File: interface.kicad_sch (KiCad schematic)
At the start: 4 parts

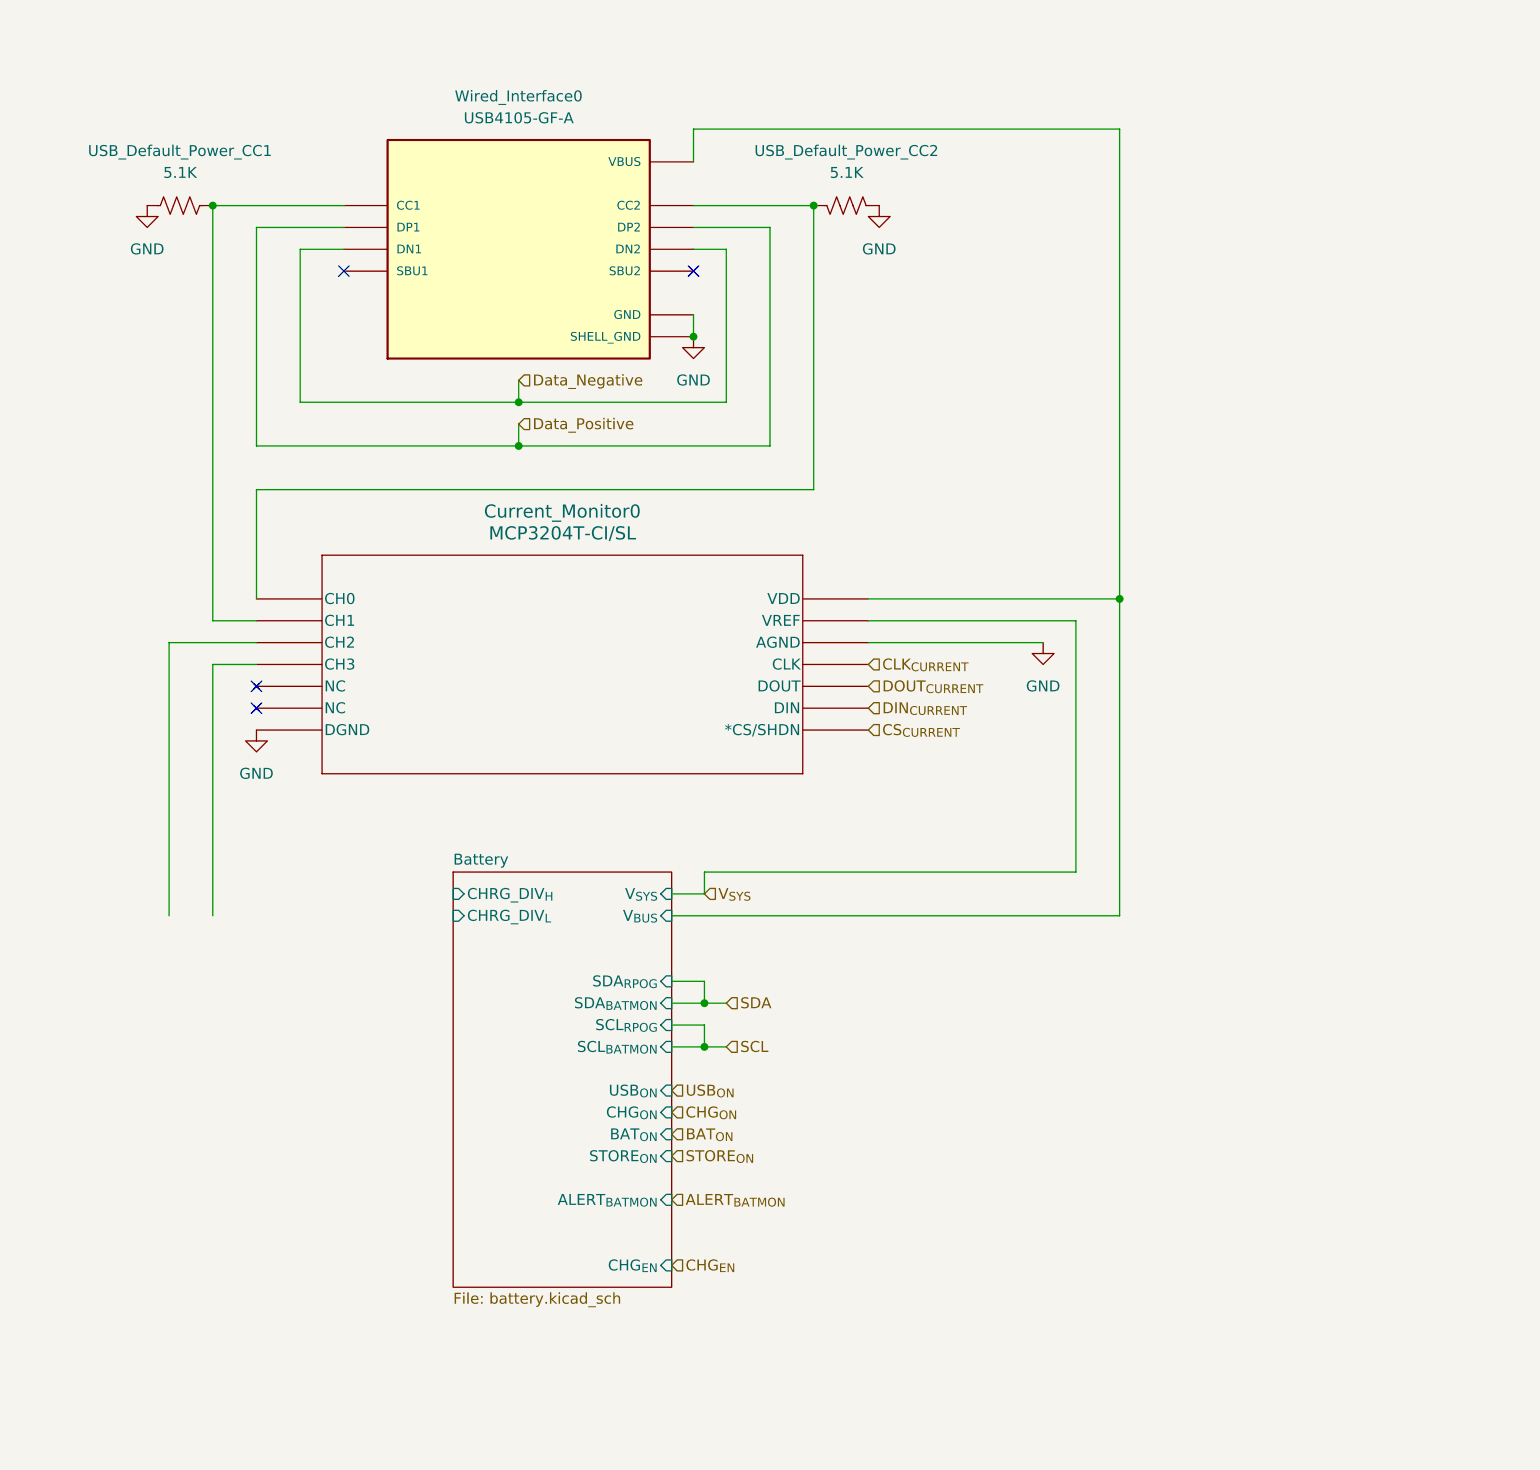
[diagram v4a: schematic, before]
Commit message: Complete most of RHS layout
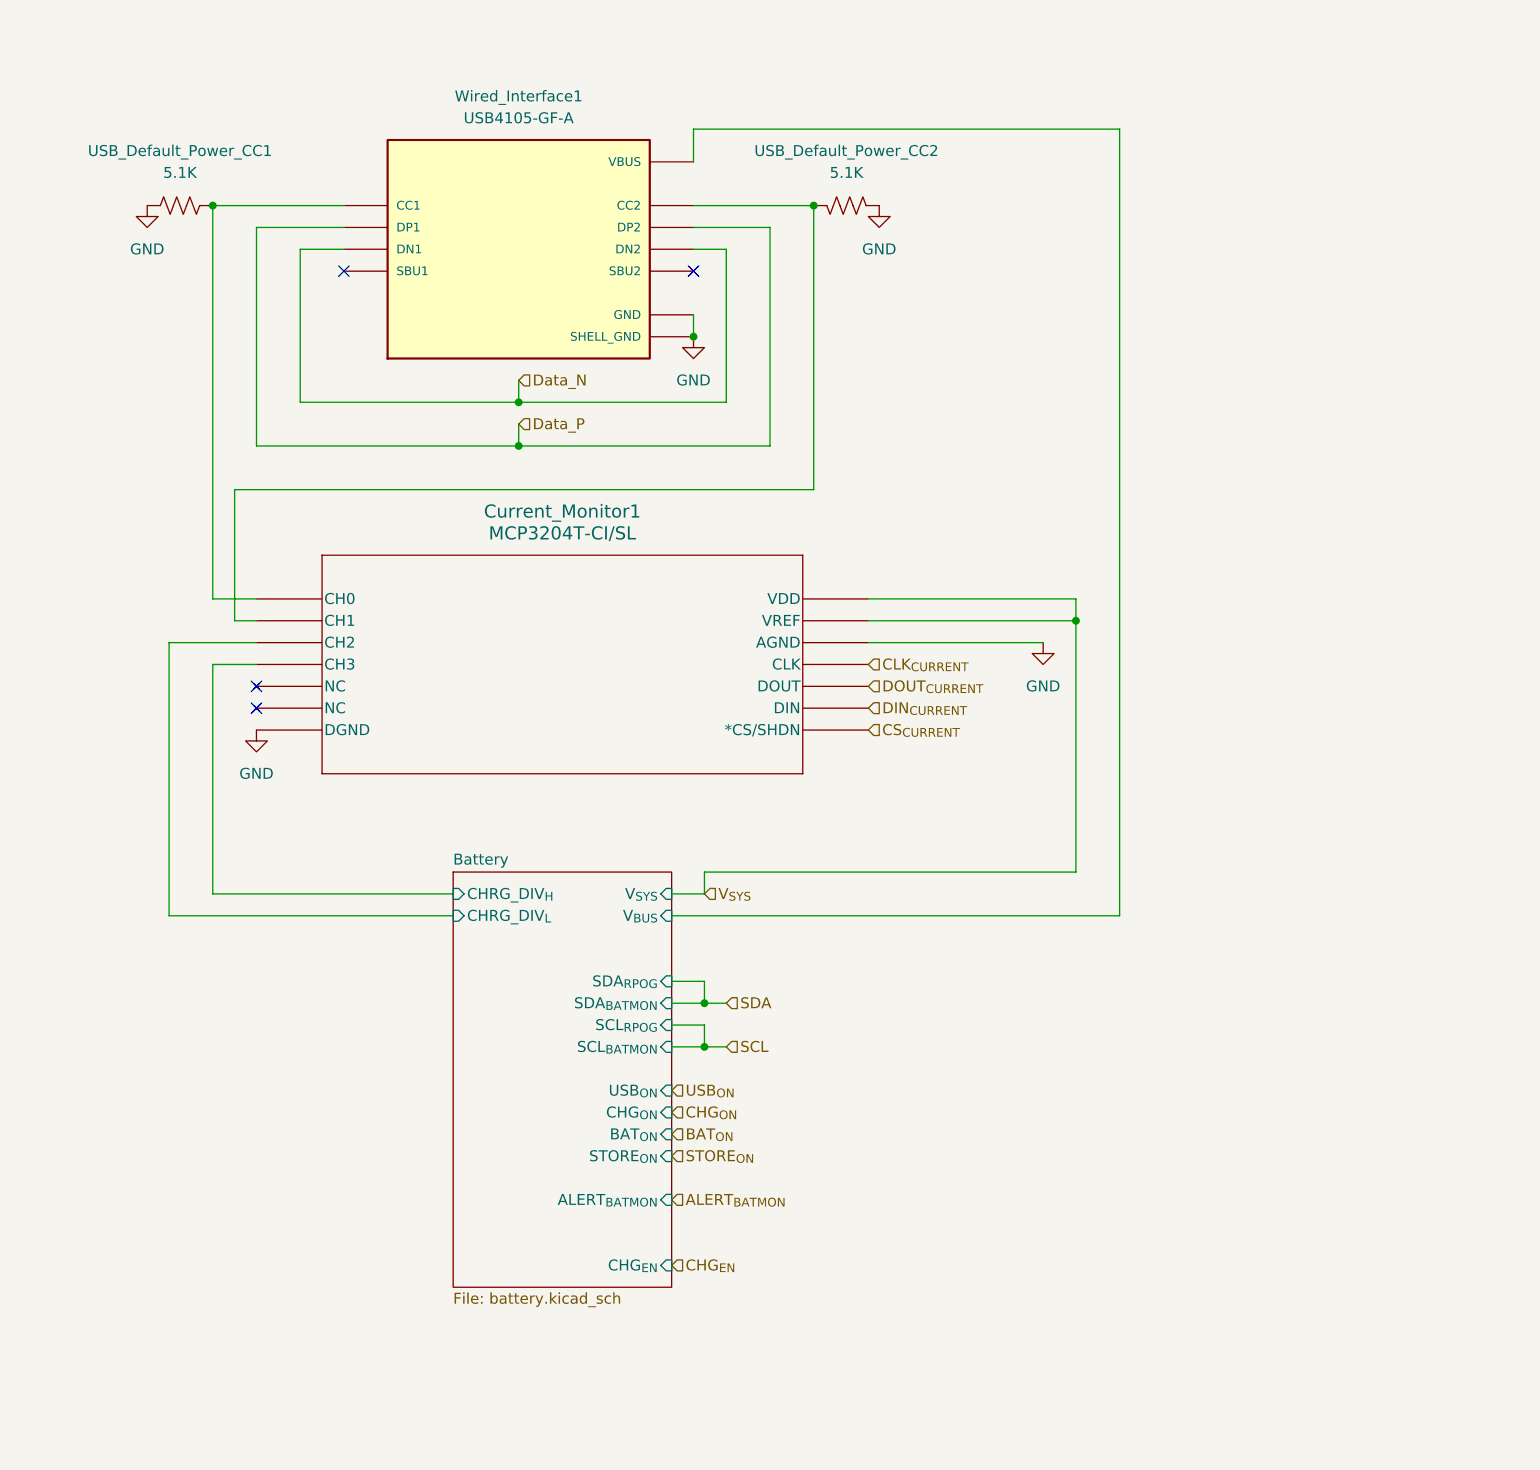
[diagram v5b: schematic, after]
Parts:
- renumbered Current_Monitor0 to Current_Monitor1, Wired_Interface0 to Wired_Interface1
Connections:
- net Battery/CHRG_DIV_{H}: now also Current_Monitor1.4 (CH3)
- net Battery/CHRG_DIV_{L}: now also Current_Monitor1.3 (CH2)
- net Battery/V_{BUS}: no longer Current_Monitor1.14 (VDD)
- net V_{SYS}: now also Current_Monitor1.14 (VDD)
- net at USB_Default_Power_CC1.1, Wired_Interface1.A5 (CC1): now also Current_Monitor1.1 (CH0); no longer Current_Monitor1.2 (CH1)
- net at USB_Default_Power_CC2.1, Wired_Interface1.B5 (CC2): now also Current_Monitor1.2 (CH1); no longer Current_Monitor1.1 (CH0)
- net Data_Negative renamed Data_N
- net Data_Positive renamed Data_P
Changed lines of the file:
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@@
-	)
-	(junction
-		(at 214.63 87.63)
-		(diameter 0)
-		(color 0 0 0 0)
 	)
 	(junction
@@
 	)
 	(junction
+		(at 209.55 90.17)
+		(diameter 0)
+		(color 0 0 0 0)
+	)
+	(junction
 		(at 144.78 64.77)
 		(diameter 0)
@@
 	(wire
 		(pts
-			(xy 114.3 87.63) (xy 114.3 74.93)
-		)
-		(stroke
-			(width 0)
-			(type default)
-		)
-	)
-	(wire
-		(pts
 			(xy 104.14 92.71) (xy 104.14 124.46)
 		)
@@
 	(wire
 		(pts
+			(xy 114.3 90.17) (xy 111.76 90.17)
+		)
+		(stroke
+			(width 0)
+			(type default)
+		)
+	)
+	(wire
+		(pts
+			(xy 109.22 87.63) (xy 114.3 87.63)
+		)
+		(stroke
+			(width 0)
+			(type default)
+		)
+	)
+	(wire
+		(pts
 			(xy 165.1 41.91) (xy 179.07 41.91)
 		)
@@
 	(wire
 		(pts
+			(xy 104.14 124.46) (xy 137.16 124.46)
+		)
+		(stroke
+			(width 0)
+			(type default)
+		)
+	)
+	(wire
+		(pts
+			(xy 111.76 74.93) (xy 179.07 74.93)
+		)
+		(stroke
+			(width 0)
+			(type default)
+		)
+	)
+	(wire
+		(pts
 			(xy 124.46 46.99) (xy 119.38 46.99)
 		)
@@
 	(wire
 		(pts
-			(xy 109.22 95.25) (xy 109.22 124.46)
+			(xy 109.22 95.25) (xy 109.22 121.92)
 		)
 		(stroke
@@
 	(wire
 		(pts
-			(xy 114.3 74.93) (xy 179.07 74.93)
-		)
-		(stroke
-			(width 0)
-			(type default)
-		)
-	)
-	(wire
-		(pts
 			(xy 209.55 119.38) (xy 209.55 90.17)
 		)
@@
 	(wire
 		(pts
+			(xy 109.22 87.63) (xy 109.22 41.91)
+		)
+		(stroke
+			(width 0)
+			(type default)
+		)
+	)
+	(wire
+		(pts
 			(xy 162.56 134.62) (xy 166.37 134.62)
 		)
@@
 	(wire
 		(pts
-			(xy 214.63 87.63) (xy 214.63 124.46)
-		)
-		(stroke
-			(width 0)
-			(type default)
-		)
-	)
-	(wire
-		(pts
 			(xy 166.37 134.62) (xy 168.91 134.62)
 		)
@@
 	(wire
 		(pts
-			(xy 185.42 87.63) (xy 214.63 87.63)
-		)
-		(stroke
-			(width 0)
-			(type default)
-		)
-	)
-	(wire
-		(pts
 			(xy 165.1 33.02) (xy 165.1 36.83)
 		)
@@
 	(wire
 		(pts
+			(xy 209.55 90.17) (xy 209.55 87.63)
+		)
+		(stroke
+			(width 0)
+			(type default)
+		)
+	)
+	(wire
+		(pts
+			(xy 111.76 90.17) (xy 111.76 74.93)
+		)
+		(stroke
+			(width 0)
+			(type default)
+		)
+	)
+	(wire
+		(pts
 			(xy 124.46 44.45) (xy 114.3 44.45)
 		)
@@
 	(wire
 		(pts
+			(xy 209.55 87.63) (xy 185.42 87.63)
+		)
+		(stroke
+			(width 0)
+			(type default)
+		)
+	)
+	(wire
+		(pts
 			(xy 162.56 137.16) (xy 166.37 137.16)
 		)
@@
 	(wire
 		(pts
-			(xy 114.3 90.17) (xy 109.22 90.17)
+			(xy 109.22 121.92) (xy 137.16 121.92)
 		)
 		(stroke
@@
 	(wire
 		(pts
-			(xy 109.22 90.17) (xy 109.22 41.91)
-		)
-		(stroke
-			(width 0)
-			(type default)
-		)
-	)
-	(wire
-		(pts
 			(xy 114.3 44.45) (xy 114.3 69.85)
 		)
@@
 	(wire
 		(pts
-			(xy 214.63 33.02) (xy 214.63 87.63)
+			(xy 214.63 33.02) (xy 214.63 124.46)
 		)
 		(stroke
@@
 		)
 	)
-	(hierarchical_label "Data_Positive"
+	(hierarchical_label "Data_P"
 		(shape input)
 		(at 144.78 67.31 0)
@@
 		)
 	)
-	(hierarchical_label "Data_Negative"
+	(hierarchical_label "Data_N"
 		(shape input)
 		(at 144.78 62.23 0)
@@
 		(dnp no)
 		(fields_autoplaced yes)
-		(property "Reference" "#PWR04"
+		(property "Reference" "#PWR0105"
 			(at 114.3 109.22 0)
 			(effects
@@
 		(dnp no)
 		(fields_autoplaced yes)
-		(property "Reference" "#PWR01"
+		(property "Reference" "#PWR0103"
 			(at 165.1 63.5 0)
 			(effects
@@
 		(dnp no)
 		(fields_autoplaced yes)
-		(property "Reference" "Current_Monitor0"
+		(property "Reference" "Current_Monitor1"
 			(at 149.86 77.47 0)
 			(effects
@@
 		(dnp no)
 		(fields_autoplaced yes)
-		(property "Reference" "#PWR03"
+		(property "Reference" "#PWR0101"
 			(at 186.69 48.26 0)
 			(effects
@@
 		(dnp no)
 		(fields_autoplaced yes)
-		(property "Reference" "#PWR05"
+		(property "Reference" "#PWR0102"
 			(at 205.74 99.06 0)
 			(effects
@@
 		(dnp no)
 		(fields_autoplaced yes)
-		(property "Reference" "#PWR02"
+		(property "Reference" "#PWR0104"
 			(at 101.6 48.26 0)
 			(effects
@@
 		(dnp no)
 		(fields_autoplaced yes)
-		(property "Reference" "Wired_Interface0"
+		(property "Reference" "Wired_Interface1"
 			(at 144.78 29.21 0)
 			(effects

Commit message: Rework right hand
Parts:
- added CR0, CR1, CR2, CR3: ESD321DYAR, SOT5x3_DYA_TEX, symbol ESD321DYAR:ESD321DYAR
- added CR4: TSD05DYFR, TVS_SOD2_DYF_TEX, symbol TSD05DYFR:TSD05DYFR
- renumbered Current_Monitor1 to Current_Monitor0, Wired_Interface1 to Wired_Interface0
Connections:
- net Battery/CHRG_DIV_{H}: now also Current_Monitor0.2 (CH1); no longer Current_Monitor0.4 (CH3)
- net Battery/CHRG_DIV_{L}: now also Current_Monitor0.1 (CH0); no longer Current_Monitor0.3 (CH2)
- net Battery/V_{BUS}: now also CR4.1 (I/O)
- net Data_N: now also CR2.1
- net Data_P: now also CR1.1
- net GND: now also CR0.2, CR1.2, CR2.2, CR3.2, CR4.2 (GND)
- net at USB_Default_Power_CC1.1, Wired_Interface0.A5 (CC1): now also Current_Monitor0.3 (CH2), CR0.1; no longer Current_Monitor0.1 (CH0)
- net at USB_Default_Power_CC2.1, Wired_Interface0.B5 (CC2): now also Current_Monitor0.4 (CH3), CR3.1; no longer Current_Monitor0.2 (CH1)
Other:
- moved on the sheet: USB_Default_Power_CC1, USB_Default_Power_CC2, Wired_Interface0
